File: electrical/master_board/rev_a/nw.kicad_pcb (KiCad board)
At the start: 2 copper layers, 42.2 x 39 mm, 1 part, among them CN70 HCSR04;F1x4H

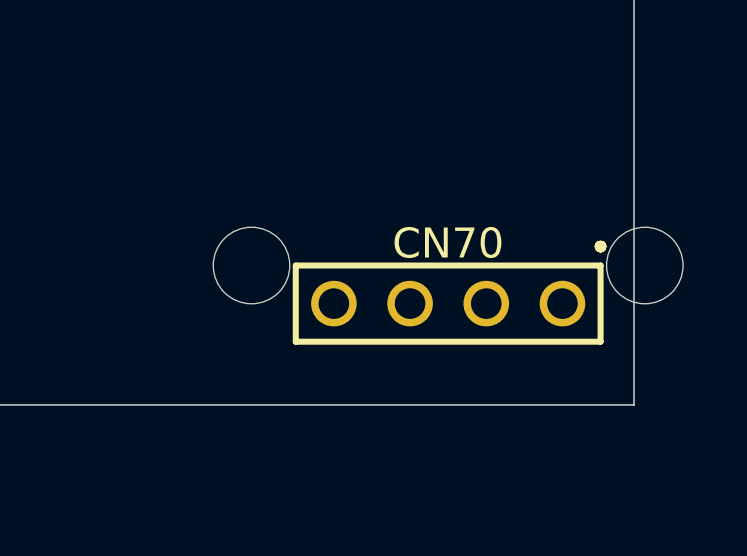
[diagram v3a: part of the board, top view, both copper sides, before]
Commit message: Finally sonars placed.  Had to manually specify the rotattions thought.
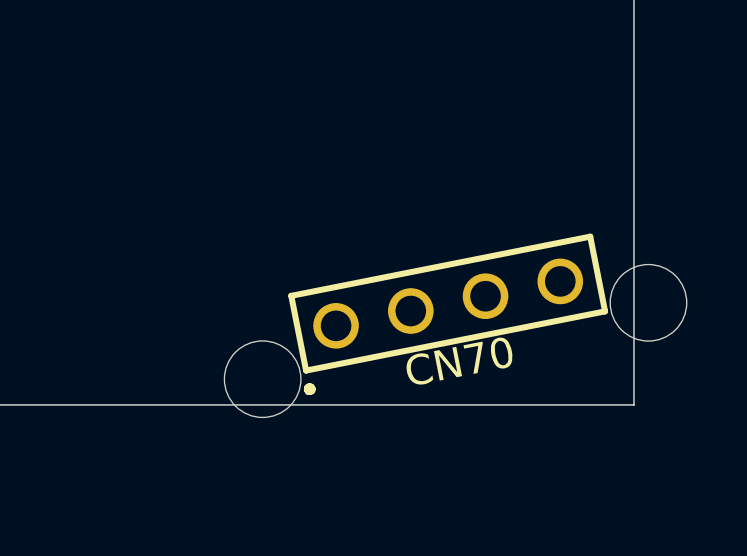
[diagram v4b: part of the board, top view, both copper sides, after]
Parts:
- turned CN70 to 191.2 degrees
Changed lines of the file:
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@@
     (uvia_dia 0.3)
     (uvia_drill 0.1)
-    (add_net "Net-(CN70-Pad1)")
-    (add_net "Net-(CN70-Pad2)")
-    (add_net "Net-(CN70-Pad3)")
-    (add_net "Net-(CN70-Pad4)")
   )
   (module HR2:HCSR04_F1x4H (layer F.Cu)
-    (at 63.8063 57.6226)
-    (fp_text reference CN70 (at 0 -2) (layer F.SilkS)
+    (at 63.8063 57.6226 191.2)
+    (fp_text reference CN70 (at 0 -2 11.2) (layer F.SilkS)
       (effects (font (size 1 1) (thickness 0.2)))
     )
-    (fp_text value HCSR04;F1x4H (at 0 0) (layer F.Fab)
+    (fp_text value HCSR04;F1x4H (at 0 0 11.2) (layer F.Fab)
       (effects (font (size 1 1) (thickness 0.2)))
     )
+    (fp_line (start -5.08 -1.27) (end 5.08 -1.27) (layer F.SilkS) (width 0.2))
+    (fp_line (start -5.08 1.27) (end -5.08 -1.27) (layer F.SilkS) (width 0.2))
+    (fp_line (start 5.08 1.27) (end -5.08 1.27) (layer F.SilkS) (width 0.2))
     (fp_line (start 5.08 -1.27) (end 5.08 1.27) (layer F.SilkS) (width 0.2))
-    (fp_line (start 5.08 1.27) (end -5.08 1.27) (layer F.SilkS) (width 0.2))
-    (fp_line (start -5.08 1.27) (end -5.08 -1.27) (layer F.SilkS) (width 0.2))
-    (fp_line (start -5.08 -1.27) (end 5.08 -1.27) (layer F.SilkS) (width 0.2))
+    (fp_line (start 5.15 -1.83) (end 5.18 -1.91) (layer F.SilkS) (width 0.2))
+    (fp_line (start 5.08 -1.8) (end 5.15 -1.83) (layer F.SilkS) (width 0.2))
+    (fp_line (start 5.01 -1.83) (end 5.08 -1.8) (layer F.SilkS) (width 0.2))
+    (fp_line (start 4.98 -1.91) (end 5.01 -1.83) (layer F.SilkS) (width 0.2))
+    (fp_line (start 5.01 -1.98) (end 4.98 -1.91) (layer F.SilkS) (width 0.2))
+    (fp_line (start 5.08 -2) (end 5.01 -1.98) (layer F.SilkS) (width 0.2))
+    (fp_line (start 5.15 -1.98) (end 5.08 -2) (layer F.SilkS) (width 0.2))
     (fp_line (start 5.18 -1.91) (end 5.15 -1.98) (layer F.SilkS) (width 0.2))
-    (fp_line (start 5.15 -1.98) (end 5.08 -2) (layer F.SilkS) (width 0.2))
-    (fp_line (start 5.08 -2) (end 5.01 -1.98) (layer F.SilkS) (width 0.2))
-    (fp_line (start 5.01 -1.98) (end 4.98 -1.91) (layer F.SilkS) (width 0.2))
-    (fp_line (start 4.98 -1.91) (end 5.01 -1.83) (layer F.SilkS) (width 0.2))
-    (fp_line (start 5.01 -1.83) (end 5.08 -1.8) (layer F.SilkS) (width 0.2))
-    (fp_line (start 5.08 -1.8) (end 5.15 -1.83) (layer F.SilkS) (width 0.2))
-    (fp_line (start 5.15 -1.83) (end 5.18 -1.91) (layer F.SilkS) (width 0.2))
-    (pad "HCSR04 West Tie Down Hole" np_thru_hole circle (at -6.555 -1.27) (size 2.55 2.55) (drill 2.55) (layers *.Cu *.Mask))
-    (pad "HCSR04 East Tie Down Hole" np_thru_hole circle (at 6.555 -1.27) (size 2.55 2.55) (drill 2.55) (layers *.Cu *.Mask))
-    (pad 4 thru_hole circle (at -3.81 0) (size 1.52 1.52) (drill 1.02) (layers *.Cu *.Mask))
-    (pad 3 thru_hole circle (at -1.27 0) (size 1.52 1.52) (drill 1.02) (layers *.Cu *.Mask))
-    (pad 2 thru_hole circle (at 1.27 0) (size 1.52 1.52) (drill 1.02) (layers *.Cu *.Mask))
-    (pad 1 thru_hole circle (at 3.81 0) (size 1.52 1.52) (drill 1.02) (layers *.Cu *.Mask))
+    (pad "HCSR04 West Tie Down Hole" np_thru_hole circle (at -6.555 -1.27 191.2) (size 2.55 2.55) (drill 2.55) (layers *.Cu *.Mask))
+    (pad "HCSR04 East Tie Down Hole" np_thru_hole circle (at 6.555 -1.27 191.2) (size 2.55 2.55) (drill 2.55) (layers *.Cu *.Mask))
+    (pad 4 thru_hole circle (at -3.81 0 191.2) (size 1.52 1.52) (drill 1.02) (layers *.Cu *.Mask))
+    (pad 3 thru_hole circle (at -1.27 0 191.2) (size 1.52 1.52) (drill 1.02) (layers *.Cu *.Mask))
+    (pad 2 thru_hole circle (at 1.27 0 191.2) (size 1.52 1.52) (drill 1.02) (layers *.Cu *.Mask))
+    (pad 1 thru_hole circle (at 3.81 0 191.2) (size 1.52 1.52) (drill 1.02) (layers *.Cu *.Mask))
   )
   (gr_line (start 70 61) (end 70 26.46) (layer Edge.Cuts) (width 0.05))
